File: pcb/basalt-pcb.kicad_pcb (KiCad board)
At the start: 2 copper layers, 29 x 42 mm, 12 parts, among them J1 Conn_01x08_Pin, J2 Conn_01x08_Pin, J3 USB4215-03-A, J4 Conn_01x04_Pin, U1 DI78L3.3ZAB, U2 STM32C071F8Px

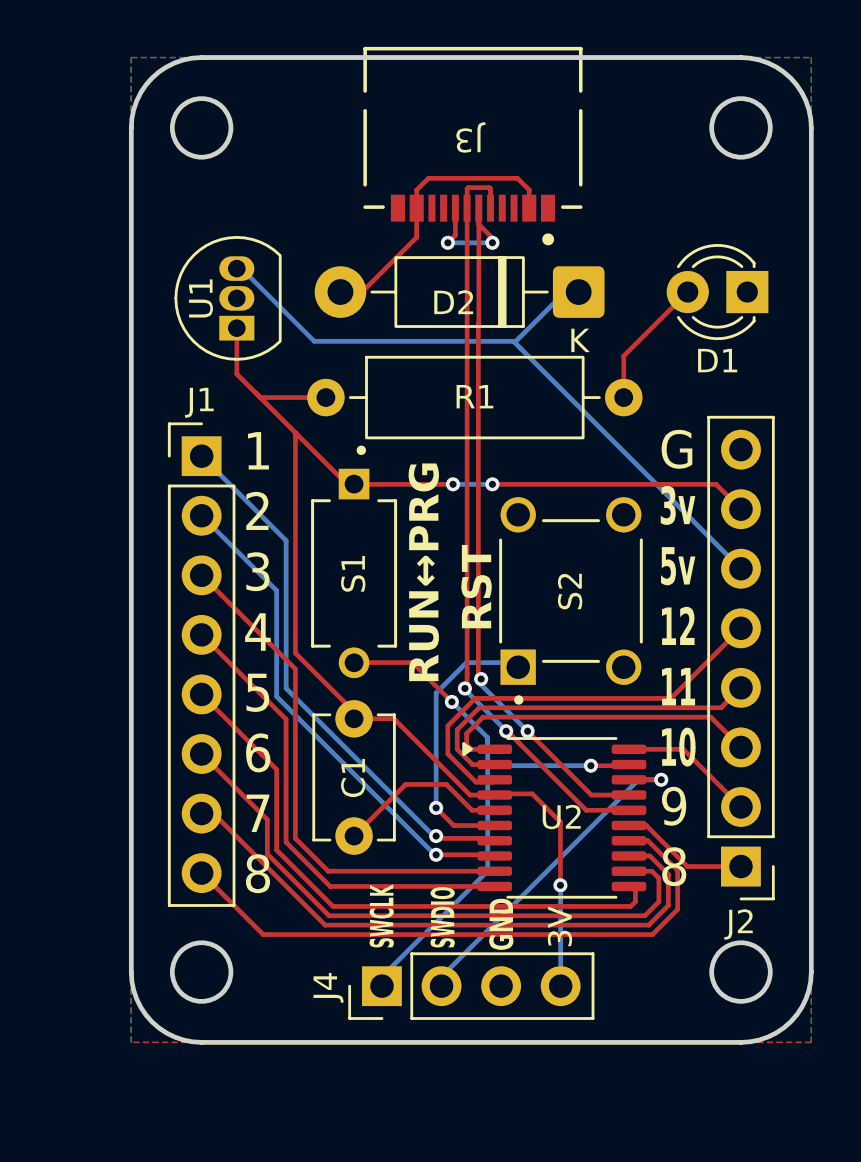
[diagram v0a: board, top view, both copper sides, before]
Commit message: Update with new pin count (removing pins that cannot be accessed with existing arduino ide variant), start work on arduino board config
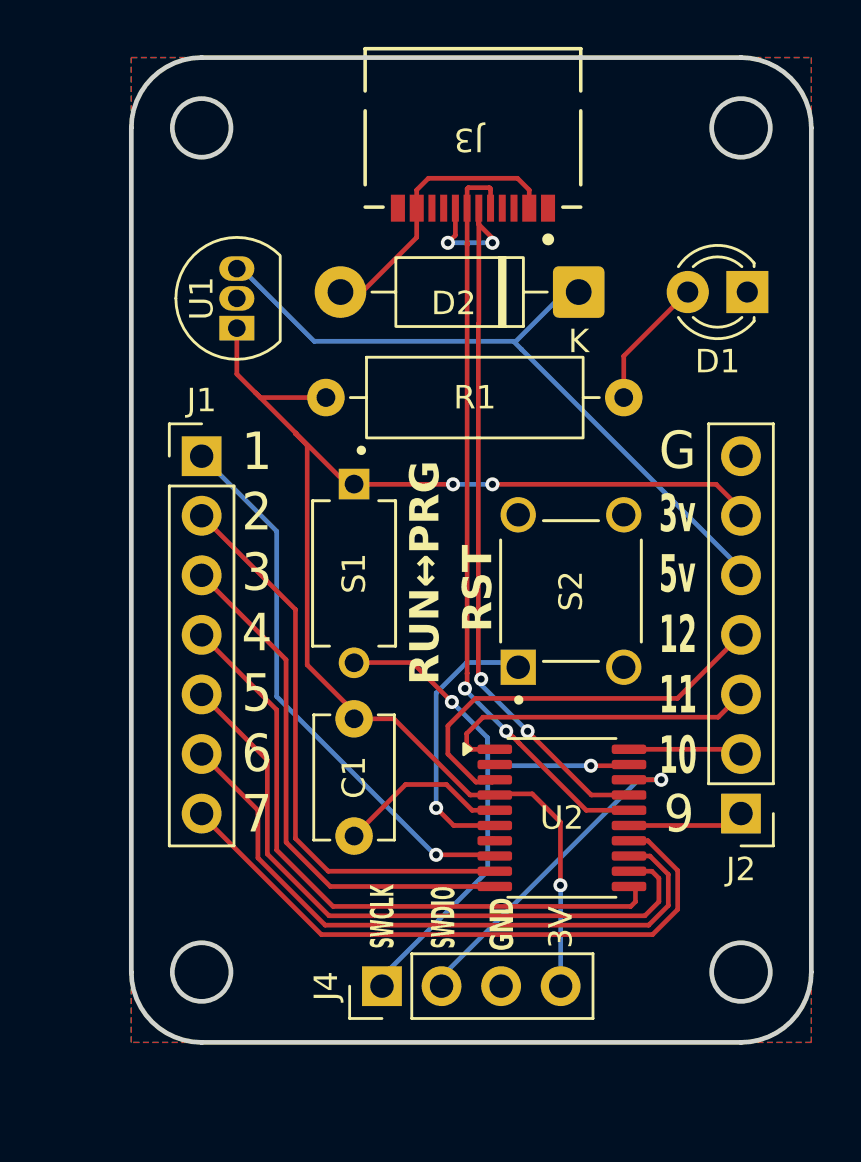
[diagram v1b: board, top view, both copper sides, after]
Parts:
- J1, J2: value Conn_01x08_Pin -> Conn_01x07_Pin; footprint Connector_PinHeader_2.54mm:PinHeader_1x08_P2.54mm_Vertical -> Connector_PinHeader_2.54mm:PinHeader_1x07_P2.54mm_Vertical
- moved J2 2.26 mm to (161.0, 109.2)
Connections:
- J2 pad 5: Net-(J2-Pin_5) -> +5V
- J2 pad 6: +5V -> +3.3V
- J2 pad 7: +3.3V -> GND
- U2 pad 10: Net-(J1-Pin_4) -> Net-(J1-Pin_3)
- U2 pad 11: Net-(J1-Pin_5) -> Net-(J1-Pin_4)
- U2 pad 12: Net-(J1-Pin_6) -> Net-(J1-Pin_5)
- U2 pad 13: Net-(J1-Pin_7) -> Net-(J1-Pin_6)
- U2 pad 14: Net-(J1-Pin_8) -> Net-(J1-Pin_7)
- U2 pad 2: Net-(J2-Pin_4) -> unconnected-(U2-PC14-Pad2)
- U2 pad 3: Net-(J2-Pin_5) -> Net-(J2-Pin_4)
- U2 pad 7: Net-(J1-Pin_1) -> unconnected-(U2-PA0-Pad7)
- U2 pad 8: Net-(J1-Pin_2) -> Net-(J1-Pin_1)
- U2 pad 9: Net-(J1-Pin_3) -> Net-(J1-Pin_2)
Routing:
- net Net-(J1-Pin_8): track 26.1 -> 0.00 mm
- net Net-(J2-Pin_5): track 18.0 -> 0.00 mm
- net Net-(J1-Pin_4): track 20.2 -> 28.2 mm
- net Net-(J1-Pin_5): track 25.5 -> 28.9 mm
- net Net-(J1-Pin_2): track 21.2 -> 24.5 mm, vias 1 -> 0
- net Net-(J2-Pin_4): track 15.7 -> 17.8 mm
- net Net-(J1-Pin_7): track 25.6 -> 27.7 mm
- net Net-(J1-Pin_6): track 26.4 -> 27.9 mm
- net Net-(J2-Pin_2): track 5.79 -> 5.05 mm
- net Net-(J1-Pin_1): track 23.0 -> 23.7 mm
- net Net-(J1-Pin_3): track 22.3 -> 22.9 mm
- net Net-(J2-Pin_1): track 5.51 -> 4.99 mm
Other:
- board text added: "1 2 3 4 5 6 7"
- board text added: "9"
- board text removed: "1 2 3 4 5 6 7 8"
- board text removed: "9 8"

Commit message: Add 3D models and 3D model images to README
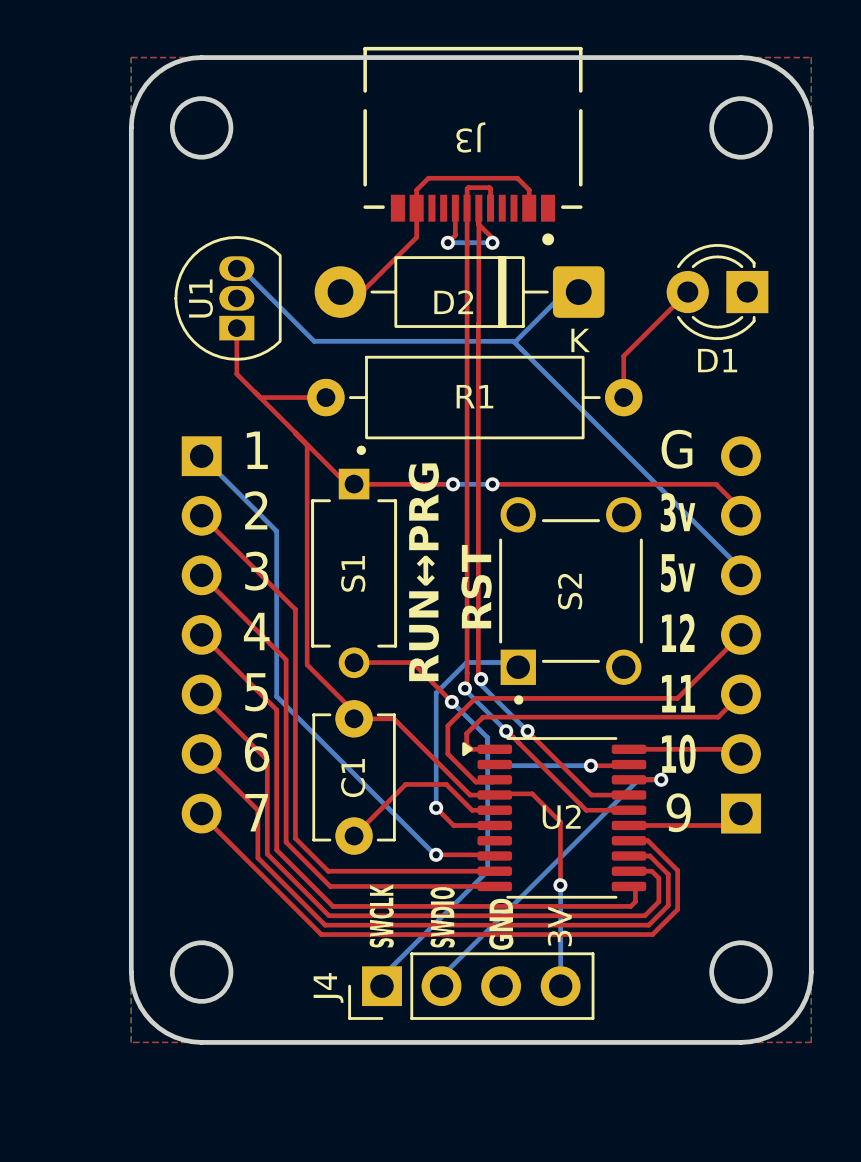
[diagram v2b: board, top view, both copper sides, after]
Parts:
- J1, J2: moved to B.Cu
- turned J1 to 180 degrees
- turned J2 to 0 degrees

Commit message: Increase power trace widths
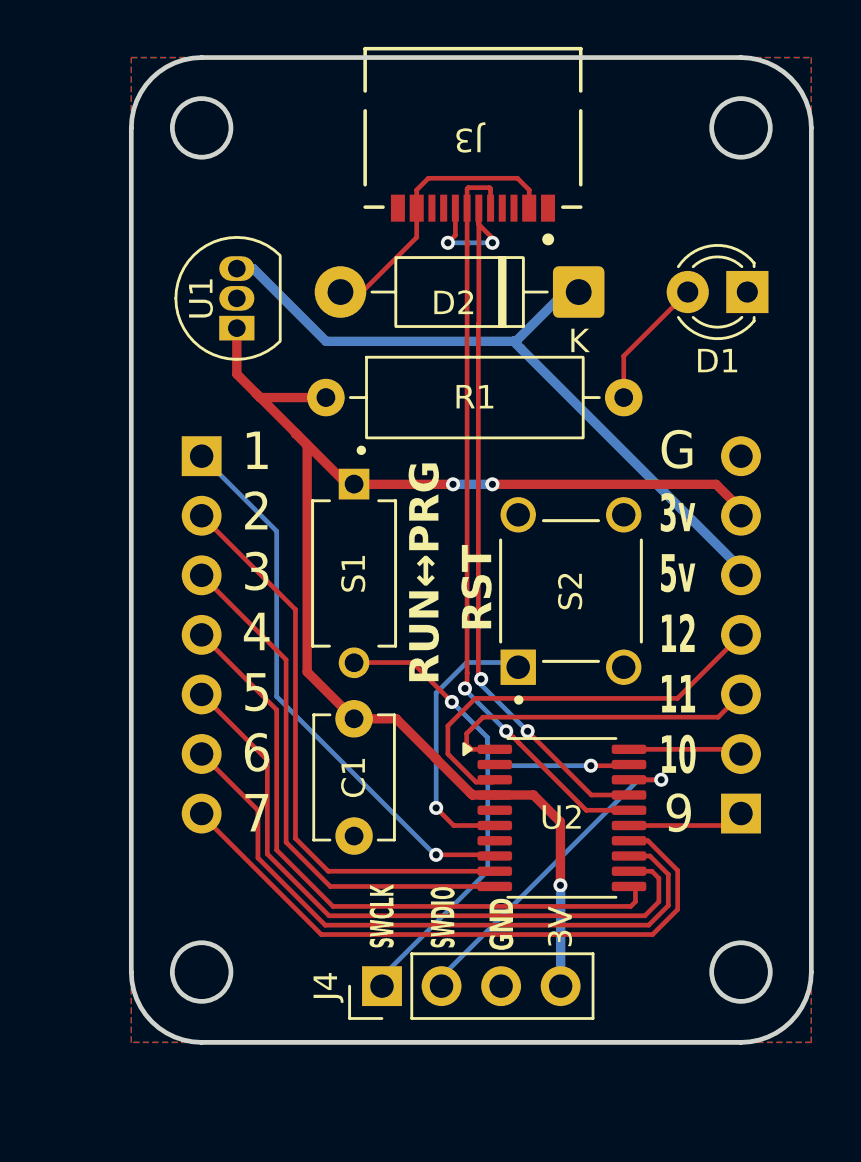
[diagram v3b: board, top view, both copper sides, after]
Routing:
- net GND: track 7.37 -> 0.00 mm
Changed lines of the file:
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@@
 	)
 	(segment
-		(start 144.5 104.9)
-		(end 144.5 105.2)
-		(width 0.2)
-		(layer "F.Cu")
-		(net "+3.3V")
-	)
-	(segment
-		(start 142.5 93.54)
-		(end 142.5 102.9)
-		(width 0.2)
-		(layer "F.Cu")
-		(net "+3.3V")
-	)
-	(segment
-		(start 146.2 105.2)
-		(end 144.5 105.2)
-		(width 0.2)
-		(layer "F.Cu")
-		(net "+3.3V")
-	)
-	(segment
-		(start 153.3 109.6)
-		(end 152.1 108.4)
-		(width 0.2)
+		(start 149.55 108.45)
+		(end 149.5 108.4)
+		(width 0.4)
 		(layer "F.Cu")
 		(net "+3.3V")
@@
 		(start 142.04 93.04)
 		(end 144.19 95.19)
-		(width 0.2)
+		(width 0.4)
 		(layer "F.Cu")
 		(net "+3.3V")
@@
 		(start 144.51 95.2)
 		(end 144.5 95.19)
-		(width 0.2)
+		(width 0.4)
 		(layer "F.Cu")
 		(net "+3.3V")
@@
 		(start 142 93)
 		(end 140.3 91.3)
-		(width 0.2)
+		(width 0.4)
 		(layer "F.Cu")
 		(net "+3.3V")
@@
 		(start 150.4 95.2)
 		(end 159.94 95.2)
-		(width 0.2)
+		(width 0.4)
+		(layer "F.Cu")
+		(net "+3.3V")
+	)
+	(segment
+		(start 152.15 108.45)
+		(end 150.5 108.45)
+		(width 0.4)
+		(layer "F.Cu")
+		(net "+3.3V")
+	)
+	(segment
+		(start 150.5 108.45)
+		(end 149.55 108.45)
+		(width 0.4)
+		(layer "F.Cu")
+		(net "+3.3V")
+	)
+	(segment
+		(start 148 106.9)
+		(end 146.3 105.2)
+		(width 0.4)
+		(layer "F.Cu")
+		(net "+3.3V")
+	)
+	(segment
+		(start 140.3 91.3)
+		(end 140.5 91.5)
+		(width 0.4)
+		(layer "F.Cu")
+		(net "+3.3V")
+	)
+	(segment
+		(start 159.94 95.2)
+		(end 161 96.26)
+		(width 0.4)
 		(layer "F.Cu")
 		(net "+3.3V")
@@
 		(start 142 93.04)
 		(end 142.5 93.54)
-		(width 0.2)
-		(layer "F.Cu")
-		(net "+3.3V")
-	)
-	(segment
-		(start 140.3 91.3)
-		(end 140.5 91.5)
-		(width 0.2)
-		(layer "F.Cu")
-		(net "+3.3V")
-	)
-	(segment
-		(start 159.94 95.2)
-		(end 161 96.26)
-		(width 0.2)
-		(layer "F.Cu")
-		(net "+3.3V")
-	)
-	(segment
-		(start 152.1 108.4)
-		(end 150.55 108.4)
-		(width 0.2)
+		(width 0.4)
 		(layer "F.Cu")
 		(net "+3.3V")
@@
 		(start 148.720032 95.2)
 		(end 144.51 95.2)
-		(width 0.2)
+		(width 0.4)
+		(layer "F.Cu")
+		(net "+3.3V")
+	)
+	(segment
+		(start 149.492893 108.4)
+		(end 148 106.907106)
+		(width 0.4)
 		(layer "F.Cu")
 		(net "+3.3V")
@@
 		(start 142 93.04)
 		(end 142.04 93.04)
-		(width 0.2)
+		(width 0.4)
+		(layer "F.Cu")
+		(net "+3.3V")
+	)
+	(segment
+		(start 140.5 91.5)
+		(end 143.3 91.5)
+		(width 0.4)
+		(layer "F.Cu")
+		(net "+3.3V")
+	)
+	(segment
+		(start 142.5 103.2)
+		(end 144.5 105.2)
+		(width 0.4)
+		(layer "F.Cu")
+		(net "+3.3V")
+	)
+	(segment
+		(start 140.3 91.3)
+		(end 139.5 90.5)
+		(width 0.4)
+		(layer "F.Cu")
+		(net "+3.3V")
+	)
+	(segment
+		(start 142 93.04)
+		(end 142 93)
+		(width 0.4)
+		(layer "F.Cu")
+		(net "+3.3V")
+	)
+	(segment
+		(start 146.3 105.2)
+		(end 144.5 105.2)
+		(width 0.4)
 		(layer "F.Cu")
 		(net "+3.3V")
@@
 		(start 153.3 112.3)
 		(end 153.3 109.6)
-		(width 0.2)
-		(layer "F.Cu")
-		(net "+3.3V")
-	)
-	(segment
-		(start 140.5 91.5)
-		(end 143.3 91.5)
-		(width 0.2)
-		(layer "F.Cu")
-		(net "+3.3V")
-	)
-	(segment
-		(start 142.5 102.9)
-		(end 144.5 104.9)
-		(width 0.2)
-		(layer "F.Cu")
-		(net "+3.3V")
-	)
-	(segment
-		(start 140.3 91.3)
-		(end 139.5 90.5)
-		(width 0.2)
-		(layer "F.Cu")
-		(net "+3.3V")
-	)
-	(segment
-		(start 142 93.04)
-		(end 142 93)
-		(width 0.2)
+		(width 0.4)
+		(layer "F.Cu")
+		(net "+3.3V")
+	)
+	(segment
+		(start 142.5 93.54)
+		(end 142.5 103.2)
+		(width 0.4)
 		(layer "F.Cu")
 		(net "+3.3V")
@@
 		(start 143 91.75)
 		(end 143 91.5)
-		(width 0.2)
-		(layer "F.Cu")
-		(net "+3.3V")
-	)
-	(segment
-		(start 150.5 108.45)
-		(end 149.45 108.45)
-		(width 0.2)
+		(width 0.4)
+		(layer "F.Cu")
+		(net "+3.3V")
+	)
+	(segment
+		(start 148 106.907106)
+		(end 148 106.9)
+		(width 0.4)
+		(layer "F.Cu")
+		(net "+3.3V")
+	)
+	(segment
+		(start 149.5 108.4)
+		(end 149.492893 108.4)
+		(width 0.4)
 		(layer "F.Cu")
 		(net "+3.3V")
@@
 		(start 139.5 90.5)
 		(end 139.5 88.54)
-		(width 0.2)
-		(layer "F.Cu")
-		(net "+3.3V")
-	)
-	(segment
-		(start 150.55 108.4)
-		(end 150.5 108.45)
-		(width 0.2)
+		(width 0.4)
 		(layer "F.Cu")
 		(net "+3.3V")
@@
 		(start 144.19 95.19)
 		(end 144.5 95.19)
-		(width 0.2)
-		(layer "F.Cu")
-		(net "+3.3V")
-	)
-	(segment
-		(start 149.45 108.45)
-		(end 146.2 105.2)
-		(width 0.2)
+		(width 0.4)
+		(layer "F.Cu")
+		(net "+3.3V")
+	)
+	(segment
+		(start 153.3 109.6)
+		(end 152.15 108.45)
+		(width 0.4)
 		(layer "F.Cu")
 		(net "+3.3V")
@@
 		(drill 0.3)
 		(layers "F.Cu" "B.Cu")
-		(capping no)
-		(covering
-			(front no)
-			(back no)
-		)
-		(plugging
-			(front no)
-			(back no)
-		)
-		(filling no)
 		(net "+3.3V")
 	)
@@
 		(start 148.720032 95.2)
 		(end 150.4 95.2)
-		(width 0.2)
+		(width 0.4)
 		(layer "B.Cu")
 		(net "+3.3V")
@@
 		(start 153.31 112.31)
 		(end 153.31 116.6)
-		(width 0.2)
+		(width 0.4)
 		(layer "B.Cu")
 		(net "+3.3V")
@@
 		(start 153.31 116.6)
 		(end 152.91 116.6)
-		(width 0.2)
+		(width 0.4)
 		(layer "B.Cu")
 		(net "+3.3V")
@@
 		(start 153.3 112.3)
 		(end 153.31 112.31)
-		(width 0.2)
-		(layer "B.Cu")
-		(net "+3.3V")
-	)
-	(segment
-		(start 149.534314 109.1)
-		(end 148.434314 108)
-		(width 0.2)
-		(layer "F.Cu")
-		(net "GND")
-	)
-	(segment
-		(start 146.7 108)
-		(end 144.5 110.2)
-		(width 0.2)
-		(layer "F.Cu")
-		(net "GND")
-	)
-	(segment
-		(start 150.5 109.1)
-		(end 149.534314 109.1)
-		(width 0.2)
-		(layer "F.Cu")
-		(net "GND")
-	)
-	(segment
-		(start 148.434314 108)
-		(end 146.7 108)
-		(width 0.2)
-		(layer "F.Cu")
-		(net "GND")
+		(width 0.4)
+		(layer "B.Cu")
+		(net "+3.3V")
 	)
 	(segment
@@
 		(start 151.4 89.1)
 		(end 151.3 89.1)
-		(width 0.2)
+		(width 0.4)
 		(layer "B.Cu")
 		(net "+5V")
@@
 		(start 151.64 89.44)
 		(end 161 98.8)
-		(width 0.2)
+		(width 0.4)
+		(layer "B.Cu")
+		(net "+5V")
+	)
+	(segment
+		(start 139.5 86)
+		(end 140.2 86)
+		(width 0.4)
+		(layer "B.Cu")
+		(net "+5V")
+	)
+	(segment
+		(start 140.2 86)
+		(end 143.3 89.1)
+		(width 0.4)
 		(layer "B.Cu")
 		(net "+5V")
@@
 		(start 151.3 89.1)
 		(end 151.64 89.44)
-		(width 0.2)
-		(layer "B.Cu")
-		(net "+5V")
-	)
-	(segment
-		(start 142.8 89.1)
-		(end 151.3 89.1)
-		(width 0.2)
+		(width 0.4)
 		(layer "B.Cu")
 		(net "+5V")
@@
 		(start 153.5 87)
 		(end 151.4 89.1)
-		(width 0.2)
-		(layer "B.Cu")
-		(net "+5V")
-	)
-	(segment
-		(start 139.5 86)
-		(end 139.7 86)
-		(width 0.2)
+		(width 0.4)
 		(layer "B.Cu")
 		(net "+5V")
@@
 		(start 154.08 87)
 		(end 153.5 87)
-		(width 0.2)
+		(width 0.4)
 		(layer "B.Cu")
 		(net "+5V")
 	)
 	(segment
-		(start 139.7 86)
-		(end 142.8 89.1)
-		(width 0.2)
+		(start 143.3 89.1)
+		(end 151.3 89.1)
+		(width 0.4)
 		(layer "B.Cu")
 		(net "+5V")

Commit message: Small tweaks to PCB, add logo, etc.
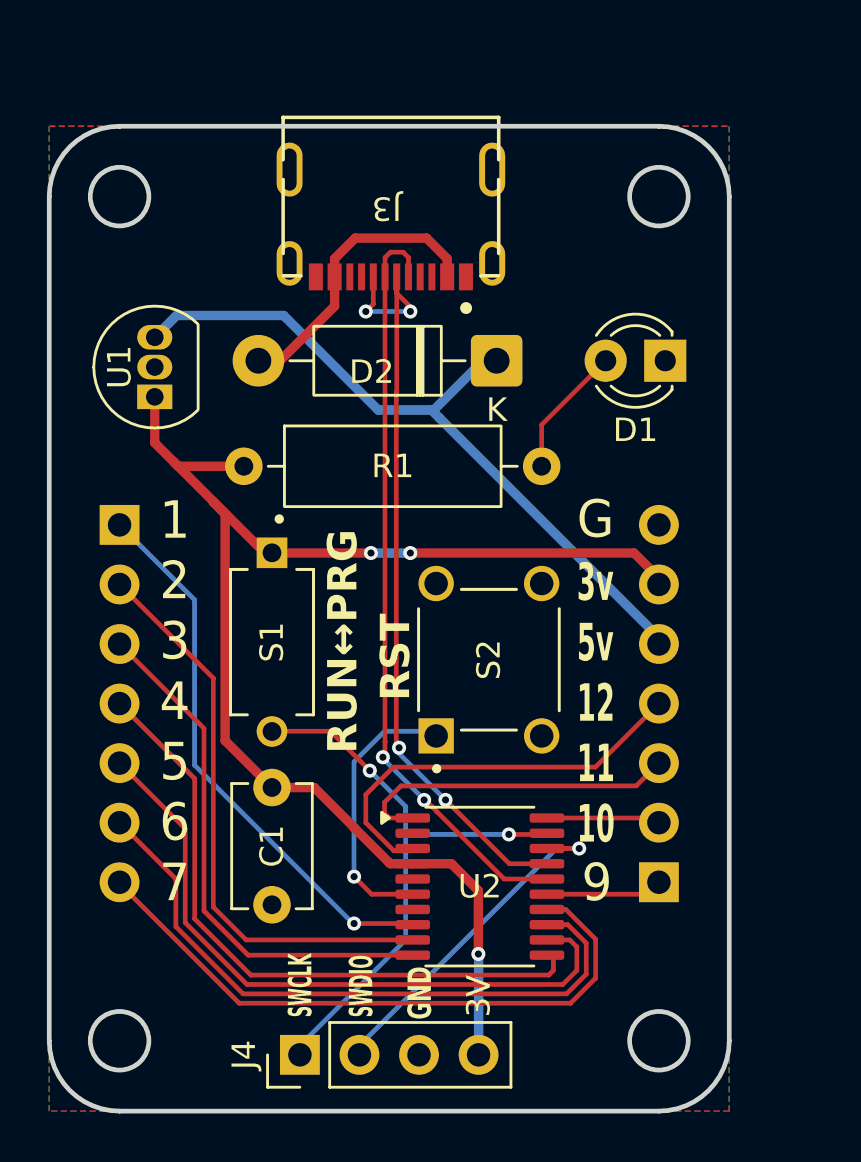
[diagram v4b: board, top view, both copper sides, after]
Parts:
- moved D1 4.56 mm to (157.8, 89.9)
- moved D2 4.56 mm to (150.6, 89.9)
- moved J1 4.56 mm to (134.5, 96.9)
- moved J2 4.56 mm to (157.5, 112.2)
- moved J3 4.56 mm to (146.1, 82.9)
- moved J4 4.56 mm to (142.2, 119.5)
- moved R1 4.56 mm to (139.8, 94.4)
- moved S1 4.56 mm to (141.0, 101.9)
- moved S2 4.56 mm to (150.2, 102.7)
- moved U2 4.56 mm to (149.9, 112.4)
- moved C1 4.56 mm to (141.0, 108.1)
- moved U1 4.56 mm to (136.0, 91.5)
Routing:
- net +5V: track 30.5 -> 31.2 mm
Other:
- board text added: "Basalt Rev1a"
- board text added: "github.com/oc-ece-mesa"

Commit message: Minor updates to pcb, update gitignore
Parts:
- moved C1 0.50 mm to (141.5, 108.2)
- moved U1 0.50 mm to (136.5, 91.5)
- moved D1 0.50 mm to (158.3, 90.0)
- moved D2 0.50 mm to (151.1, 90.0)
- moved J1 0.50 mm to (135.0, 97.0)
- moved J2 0.50 mm to (158.0, 112.2)
- moved J3 0.50 mm to (146.6, 83.0)
- moved J4 0.50 mm to (142.7, 119.6)
- moved R1 0.50 mm to (140.3, 94.5)
- moved S1 0.50 mm to (141.5, 102.0)
- moved S2 0.50 mm to (150.8, 102.8)
- moved U2 0.50 mm to (150.4, 112.4)

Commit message: Minor edits to pcb and titleblocks
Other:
- board text added: "Basalt Rev${REVISION}"
- board text removed: "Basalt Rev1a"
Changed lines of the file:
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@@
 		(title "MESA Basalt")
 		(date "2026-05-02")
-		(rev "2")
+		(rev "1")
 		(company "OC ECE MESA")
 	)
@@
 		)
 	)
-	(gr_text "Basalt Rev1a"
+	(gr_text "Basalt Rev${REVISION}"
 		(at 151.8 92.87 90)
 		(layer "B.SilkS")
